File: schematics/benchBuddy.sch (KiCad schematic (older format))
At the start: 0 parts

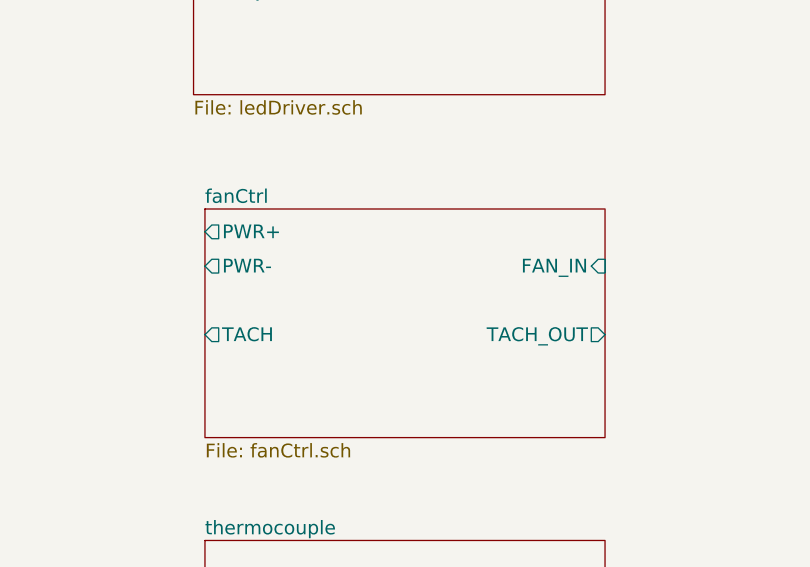
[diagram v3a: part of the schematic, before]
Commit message: added basic current source
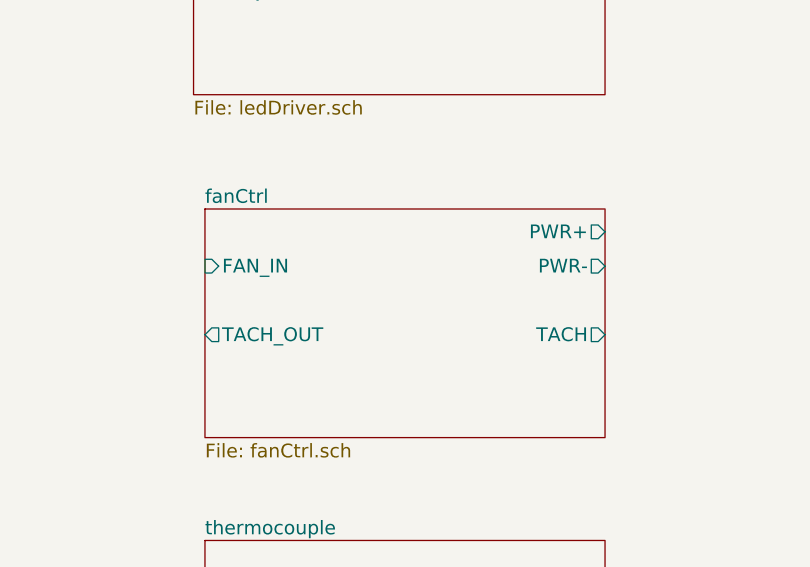
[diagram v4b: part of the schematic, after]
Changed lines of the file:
@@
-EESchema Schematic File Version 2  date Sat 05 Oct 2013 09:15:56 PM EDT
+EESchema Schematic File Version 2  date Sat 05 Oct 2013 09:39:23 PM EDT
 LIBS:power
 LIBS:device
@@
 F0 "fanCtrl" 60
 F1 "fanCtrl.sch" 60
-F2 "FAN_IN" I R 9100 3100 60
-F3 "TACH_OUT" O R 9100 3400 60
-F4 "TACH" O L 7350 3400 60
-F5 "PWR-" O L 7350 3100 60
-F6 "PWR+" O L 7350 2950 60
+F2 "FAN_IN" I L 7350 3100 60
+F3 "TACH_OUT" O L 7350 3400 60
+F4 "TACH" O R 9100 3400 60
+F5 "PWR-" O R 9100 3100 60
+F6 "PWR+" O R 9100 2950 60
 $EndSheet
 $Sheet
